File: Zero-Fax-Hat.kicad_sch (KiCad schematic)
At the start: 7 parts, among them J2 RJ11_Shielded

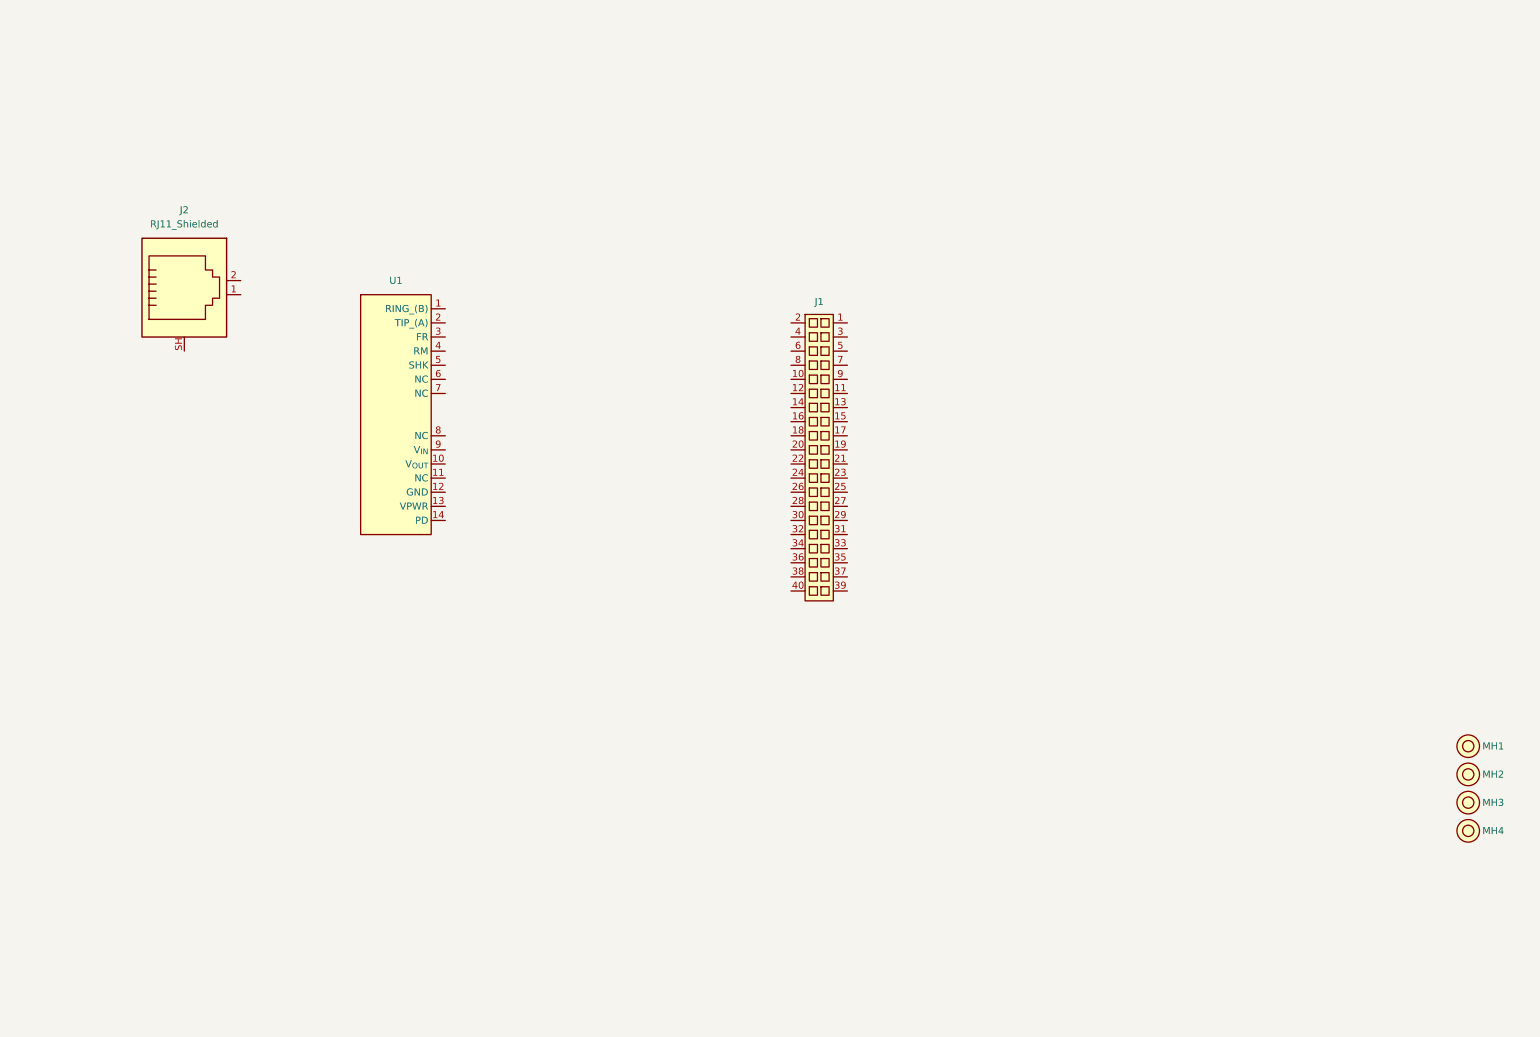
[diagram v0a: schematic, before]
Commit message: Add logic shifting circuitry, add RJ11 jack, tidy schematic
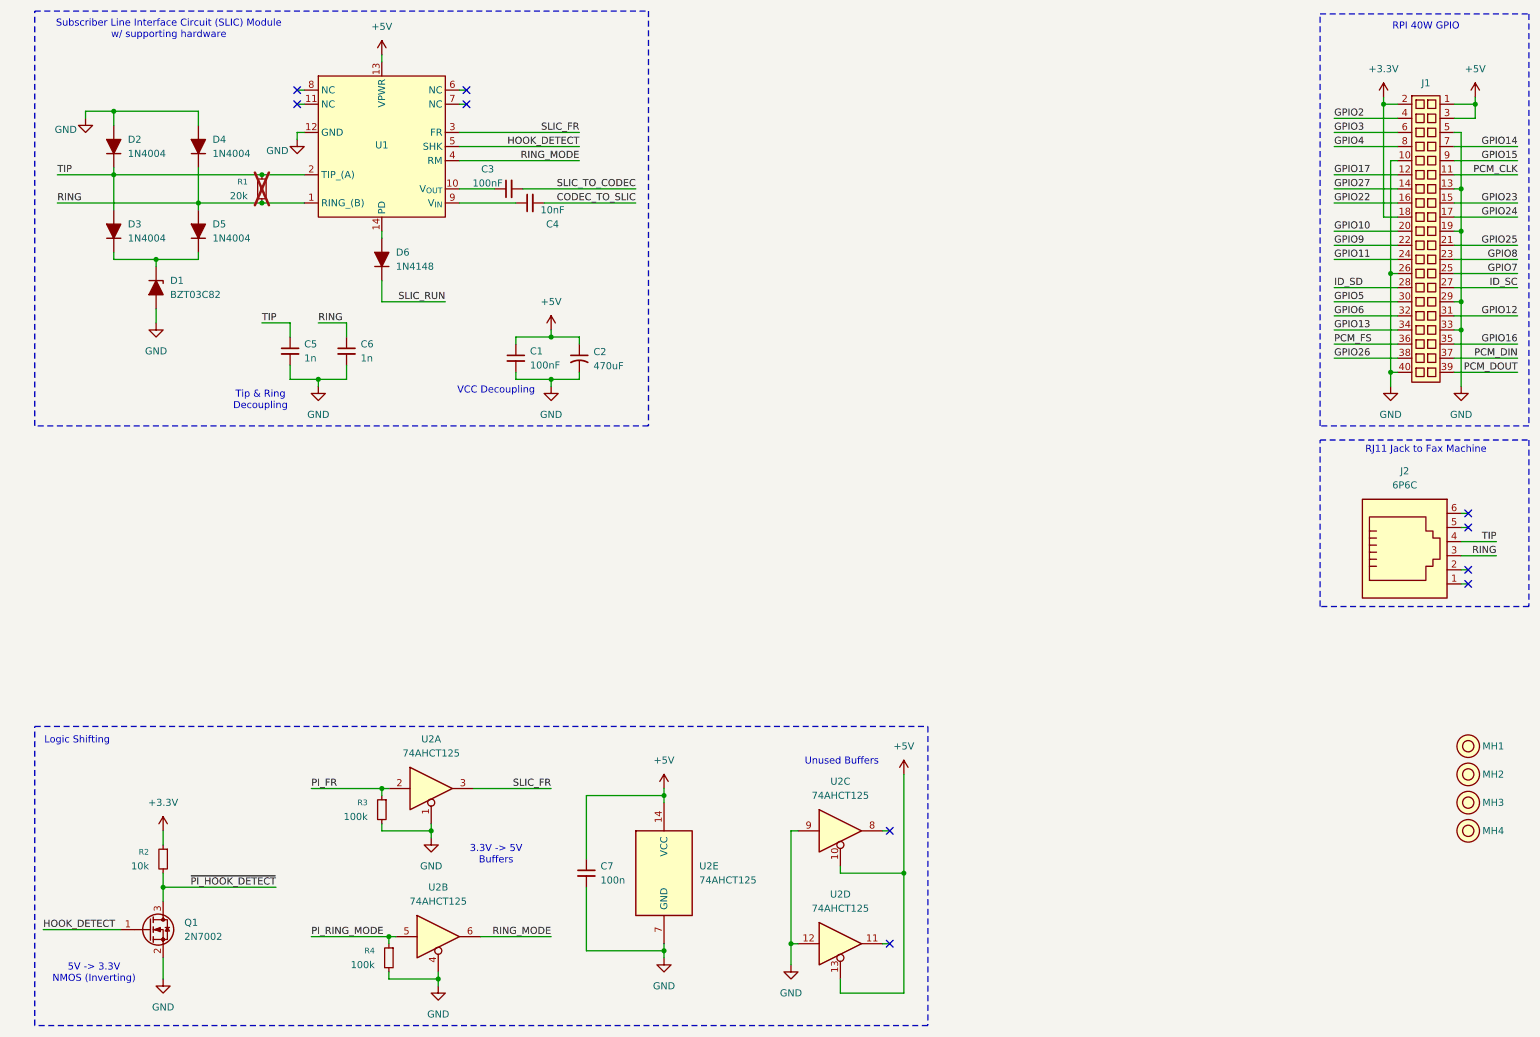
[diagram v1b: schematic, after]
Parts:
- removed J2: RJ11_Shielded, symbol Connector:RJ11_Shielded
- added C1, C3: 100nF, symbol Device:C_Small
- added C2: 470uF, symbol Device:C_Small_US
- added C4: 10nF, symbol Device:C_Small
- added C5, C6: 1n, symbol Device:C_Small
- added C7: 100n, symbol Device:C_Small
- added D1: BZT03C82, symbol Device:D_Zener_Filled
- added D2, D3, D4, D5: 1N4004, symbol Device:D_Filled
- added D6: 1N4148, symbol Device:D_Filled
- added J2: 6P6C, symbol Connector:6P6C
- added Q1: 2N7002, Package_TO_SOT_SMD:SOT-23, symbol Transistor_FET:2N7002
- added R1: 20k, symbol Device:R_Small
- added R2: 10k, symbol Device:R_Small
- added R3, R4: 100k, symbol Device:R_Small
- added U2: 74AHCT125, symbol 74xx:74AHCT125
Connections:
- net +5V: now reaches J1.1
- net +5V: now also J1.3, U1.13 (VPWR), C1.1, C2.1, C7.1, U2.10, U2.13, U2.14 (VCC)
- net GND: now reaches J1.10
- net GND: now also J1.13, J1.19, J1.26, J1.29, J1.33, J1.40, J1.5, U1.12 (GND), C1.2, C2.2, C5.2, C6.2, C7.2, D1.2 (A), D2.2 (A), D4.2 (A), Q1.2 (S), R3.2, R4.2, U2.1, U2.12, U2.4, U2.7 (GND), U2.9
- net PCM_CLK: now reaches J1.11
- net GPIO17: now reaches J1.12
- net GPIO27: now reaches J1.14
- net GPIO23: now reaches J1.15
- net GPIO22: now reaches J1.16
- net GPIO24: now reaches J1.17
- net +3.3V: now reaches J1.18
- net +3.3V: now also J1.2, R2.1
- net GPIO10: now reaches J1.20
- net GPIO25: now reaches J1.21
- net GPIO9: now reaches J1.22
- net GPIO8: now reaches J1.23
- net GPIO11: now reaches J1.24
- net GPIO7: now reaches J1.25
- net ID_SC: now reaches J1.27
- net ID_SD: now reaches J1.28
- net GPIO5: now reaches J1.30
- net GPIO12: now reaches J1.31
- net GPIO6: now reaches J1.32
- net GPIO13: now reaches J1.34
- net GPIO16: now reaches J1.35
- net PCM_FS: now reaches J1.36
- net PCM_DIN: now reaches J1.37
- net GPIO26: now reaches J1.38
- net PCM_DOUT: now reaches J1.39
- net GPIO2: now reaches J1.4
- net GPIO3: now reaches J1.6
- net GPIO14: now reaches J1.7
- net GPIO4: now reaches J1.8
- net GPIO15: now reaches J1.9
- net RING: now reaches U1.1 (RING_(B))
- net RING: now also C6.1, D4.1 (K), D5.2 (A), J2.3, R1.2
- net at U1.10 (V_{OUT}): now also C3.1
- net at U1.14 (PD): now also D6.2 (A)
- net TIP: now reaches U1.2 (TIP_(A))
- net TIP: now also C5.1, D2.1 (K), D3.2 (A), J2.4, R1.1
- net SLIC_FR: now reaches U1.3 (FR)
- net SLIC_FR: now also U2.3
- net RING_MODE: now reaches U1.4 (RM)
- net RING_MODE: now also U2.6
- net HOOK_DETECT: now reaches U1.5 (SHK)
- net HOOK_DETECT: now also Q1.1 (G)
- net at U1.9 (V_{IN}): now also C4.1
- new net: D1.1 (K), D3.1 (K), D5.1 (K)
- new net CODEC_TO_SLIC: C4.2
- new net PI_FR: R3.1, U2.2
- new net PI_RING_MODE: R4.1, U2.5
- new net SLIC_RUN: D6.1 (K)
- new net SLIC_TO_CODEC: C3.2
- new net ~{PI_HOOK_DETECT}: Q1.3 (D), R2.2
- no-connect marks 0 -> 10
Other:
- note added: "3.3V -> 5V Buffers"
- note added: "5V -> 3.3V NMOS (Inverting)"
- note added: "Logic Shifting"
- note added: "RJ11 Jack to Fax Machine"
- note added: "RPI 40W GPIO"
- note added: "Subscriber Line Interface Circuit (SLIC) Module w/ supporting hardware"
- note added: "Tip & Ring Decoupling"
- note added: "Unused Buffers"
- note added: "VCC Decoupling"
- moved on the sheet: J1
